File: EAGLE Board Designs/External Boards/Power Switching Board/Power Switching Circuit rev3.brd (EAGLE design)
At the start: 93.6 x 68.1 mm, 83 parts, among them J1 CONNECTOR-3_, J2 CONNECTOR-4_SOURIAU_, J3 CONNECTOR-4_SOURIAU_, Q1 TRANSISTOR_N_MOS_2-7K1S_TK100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, Q2 TRANSISTOR_N_MOS_2-7K1S_TK100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, Q3 TRANSISTOR_N_MOS_2-7K1S_TK100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, Q4 TRANSISTOR_N_MOS_2-7K1S_TK100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, U1 LTC4421

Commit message: Replaced with new schottky diodes
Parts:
- D3, D4: value SCHOTTKY -> SCHOTTKY_SOD323_30V; device HyTechDevices:CLP1608-2L -> HyTechDevices:SOD-323
- moved D4 966.3 mm to (-25.4, -979.2), turned to 0 degrees
- moved D3 964.0 mm to (-25.4, -975.4), turned to 0 degrees
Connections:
- net GLVMS: now also D3.A; no longer D4.1
- net SHDN: now also D3.C, D4.C; no longer D3.2, D4.2
- net START: now also D4.A; no longer D3.1
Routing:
- net START: track 7.96 -> 0.15 mm
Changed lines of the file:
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@@
 <attribute name="VOLTAGE" value="15V" x="-12.954" y="5.842" size="1.778" layer="27" display="off"/>
-</element>
-<element name="D4" library="HyTechDevices" package="CLP1608-2L" value="SCHOTTKY" x="11.43" y="-13.589" smashed="yes" rot="R45">
-<attribute name="DKPN" value="112-VSKY20401608-G4-08CT-ND" x="11.43" y="-13.589" size="1.778" layer="27" rot="R45" display="off"/>
-<attribute name="MANUFACTURER" value="Vishay General Semiconductor - Diodes Division" x="11.43" y="-13.589" size="1.778" layer="27" rot="R45" display="off"/>
-<attribute name="MOPN" value="78-VSKY20401608G408" x="11.43" y="-13.589" size="1.778" layer="27" rot="R45" display="off"/>
-<attribute name="MPN" value="VSKY20401608-G4-08" x="11.43" y="-13.589" size="1.778" layer="27" rot="R45" display="off"/>
-<attribute name="NAME" x="11.070790625" y="-13.22979375" size="0.762" layer="25" font="vector" rot="R45" align="bottom-center"/>
-</element>
-<element name="D3" library="HyTechDevices" package="CLP1608-2L" value="SCHOTTKY" x="9.8552" y="-12.0142" smashed="yes" rot="R45">
-<attribute name="DKPN" value="112-VSKY20401608-G4-08CT-ND" x="9.8552" y="-12.0142" size="1.778" layer="27" rot="R45" display="off"/>
-<attribute name="MANUFACTURER" value="Vishay General Semiconductor - Diodes Division" x="9.8552" y="-12.0142" size="1.778" layer="27" rot="R45" display="off"/>
-<attribute name="MOPN" value="78-VSKY20401608G408" x="9.8552" y="-12.0142" size="1.778" layer="27" rot="R45" display="off"/>
-<attribute name="MPN" value="VSKY20401608-G4-08" x="9.8552" y="-12.0142" size="1.778" layer="27" rot="R45" display="off"/>
-<attribute name="NAME" x="9.4959875" y="-11.6549875" size="0.762" layer="25" font="vector" rot="R45" align="bottom-center"/>
 </element>
 <element name="U$1" library="HyTechDevices" package="MOUNTING_M3" value="" x="-24.511" y="-13.97" smashed="yes"/>
@@
 <attribute name="MPN" value="5015" x="-22.86" y="-971.55" size="1.778" layer="27" display="off"/>
 <attribute name="NAME" x="-22.86" y="-970.28" size="0.8128" layer="25" font="vector" align="bottom-center"/>
+</element>
+<element name="D3" library="HyTechDevices" package="SOD-323" value="SCHOTTKY_SOD323_30V" x="-25.4" y="-975.36" smashed="yes">
+<attribute name="CURRENT" value="0.8A" x="-25.4" y="-975.36" size="1.778" layer="27" display="off"/>
+<attribute name="DKPN" value="CUS08F30H3FTR-ND" x="-25.4" y="-975.36" size="1.778" layer="27" display="off"/>
+<attribute name="MANUFACTURER" value="Toshiba Semiconductor and Storage" x="-25.4" y="-975.36" size="1.778" layer="27" display="off"/>
+<attribute name="MOPN" value="757-CUS08F30H3F" x="-25.4" y="-975.36" size="1.778" layer="27" display="off"/>
+<attribute name="MPN" value="CUS08F30" x="-25.4" y="-975.36" size="1.778" layer="27" display="off"/>
+<attribute name="NAME" x="-25.4" y="-974.36" size="0.8128" layer="25" font="vector" align="bottom-center"/>
+<attribute name="VOLTAGE" value="30V" x="-25.4" y="-975.36" size="1.778" layer="27" display="off"/>
+</element>
+<element name="D4" library="HyTechDevices" package="SOD-323" value="SCHOTTKY_SOD323_30V" x="-25.4" y="-979.17" smashed="yes">
+<attribute name="CURRENT" value="0.8A" x="-25.4" y="-979.17" size="1.778" layer="27" display="off"/>
+<attribute name="DKPN" value="CUS08F30H3FTR-ND" x="-25.4" y="-979.17" size="1.778" layer="27" display="off"/>
+<attribute name="MANUFACTURER" value="Toshiba Semiconductor and Storage" x="-25.4" y="-979.17" size="1.778" layer="27" display="off"/>
+<attribute name="MOPN" value="757-CUS08F30H3F" x="-25.4" y="-979.17" size="1.778" layer="27" display="off"/>
+<attribute name="MPN" value="CUS08F30" x="-25.4" y="-979.17" size="1.778" layer="27" display="off"/>
+<attribute name="NAME" x="-25.4" y="-978.17" size="0.8128" layer="25" font="vector" align="bottom-center"/>
+<attribute name="VOLTAGE" value="30V" x="-25.4" y="-979.17" size="1.778" layer="27" display="off"/>
 </element>
 </elements>
@@
 <signal name="START">
 <contactref element="J1" pad="C"/>
-<contactref element="D3" pad="1"/>
-<wire x1="9.646603125" y1="-12.22279375" x2="4.129128125" y2="-17.74026875" width="0.6096" layer="1"/>
 <wire x1="4.129128125" y1="-17.74026875" x2="3.974496875" y2="-17.74026875" width="0.6096" layer="1"/>
+<contactref element="D4" pad="A"/>
+<wire x1="3.974496875" y1="-17.74026875" x2="-26.55" y2="-979.17" width="0" layer="19" extent="1-1"/>
 </signal>
 <signal name="OUT">
@@
 <contactref element="U1" pad="25"/>
 <contactref element="U1" pad="12"/>
-<contactref element="D3" pad="2"/>
-<contactref element="D4" pad="2"/>
 <contactref element="R15" pad="2"/>
 <contactref element="U$12" pad="2"/>
 <contactref element="D5" pad="1"/>
+<contactref element="D3" pad="C"/>
+<contactref element="D4" pad="C"/>
+<wire x1="-24.25" y1="-975.36" x2="-24.25" y2="-979.17" width="0" layer="19" extent="1-1"/>
+<wire x1="-26.225" y1="-716.28" x2="-24.25" y2="-975.36" width="0" layer="19" extent="1-1"/>
 <wire x1="-24.55" y1="-666.75" x2="-26.225" y2="-716.28" width="0" layer="19" extent="1-1"/>
 <wire x1="-24.13" y1="-488.95" x2="-24.55" y2="-666.75" width="0" layer="19" extent="1-1"/>
 <wire x1="-15.24" y1="-471.17" x2="-24.13" y2="-488.95" width="0" layer="19" extent="1-1"/>
-<wire x1="11.850728125" y1="-13.16826875" x2="-15.24" y2="-471.17" width="0" layer="19" extent="1-1"/>
-<wire x1="10.275928125" y1="-11.59346875" x2="11.850728125" y2="-13.16826875" width="0" layer="19" extent="1-1"/>
-<wire x1="8.66995625" y1="-0.675009375" x2="10.275928125" y2="-11.59346875" width="0" layer="19" extent="1-1"/>
+<wire x1="8.66995625" y1="-0.675009375" x2="-15.24" y2="-471.17" width="0" layer="19" extent="1-1"/>
 <wire x1="10.508434375" y1="1.163465625" x2="8.66995625" y2="-0.675009375" width="0" layer="19" extent="1-1"/>
 <wire x1="5.735465625" y1="5.936434375" x2="10.508434375" y2="1.163465625" width="0" layer="19" extent="1-1"/>
 </signal>
 <signal name="GLVMS">
-<contactref element="D4" pad="1"/>
 <contactref element="J1" pad="B"/>
 <wire x1="4.881634375" y1="-20.1373625" x2="4.617965625" y2="-20.1373625" width="0.6096" layer="1"/>
-<wire x1="11.221403125" y1="-13.79759375" x2="4.881634375" y2="-20.1373625" width="0" layer="19" extent="1-1"/>
+<contactref element="D3" pad="A"/>
+<wire x1="4.617965625" y1="-20.1373625" x2="-26.55" y2="-975.36" width="0" layer="19" extent="1-1"/>
 </signal>
 <signal name="N$16">

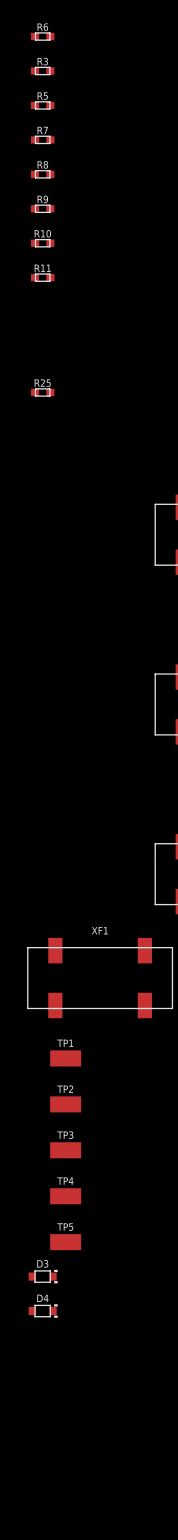
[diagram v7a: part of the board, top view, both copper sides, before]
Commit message: Replaced OV/UV resistors
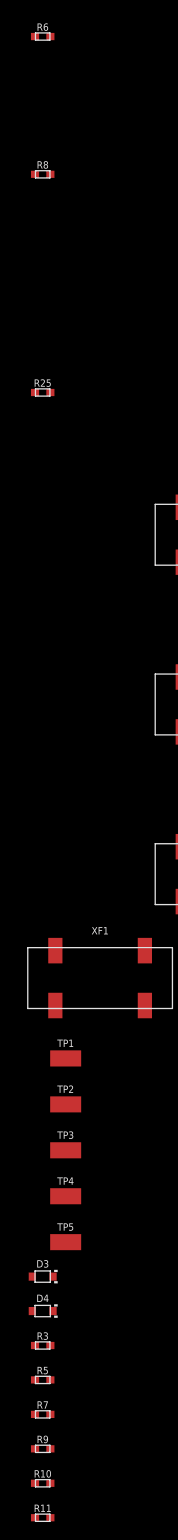
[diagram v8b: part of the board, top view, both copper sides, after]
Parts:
- R10: value RESISTOR_0603_11.8 -> RESISTOR_0603_41.2
- R11: value RESISTOR_0603_43.2 -> RESISTOR_0603_41.2
- R3: value RESISTOR_0603_5.6 -> RESISTOR_0603_5.49
- R5: value RESISTOR_0603_11.8 -> RESISTOR_0603_5.49
- R7: value RESISTOR_0603_43.2 -> RESISTOR_0603_13
- R9: value RESISTOR_0603_5.6 -> RESISTOR_0603_13
- moved R3 141.0 mm to (-25.4, -983.0)
- moved R7 141.0 mm to (-25.4, -990.6)
- moved R5 141.0 mm to (-25.4, -986.8)
- moved R10 137.2 mm to (-25.4, -998.2)
- moved R11 137.2 mm to (-25.4, -1002.0)
- moved R9 137.2 mm to (-25.4, -994.4)
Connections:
- net GND: now also R10.1; no longer R7.2
- net N$24: now also R7.2; no longer R5.2
- net N$25: now also R10.2; no longer R5.1
- net N$26: now also R5.2; no longer R9.2
- net N$27: now also R5.1, R9.2; no longer R10.2, R9.1
- net N$28: now also R9.1; no longer R10.1
